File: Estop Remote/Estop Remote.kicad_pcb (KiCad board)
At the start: 2 copper layers, 64.8 x 26.7 mm, 5 parts, among them J1 Enable Out, J2 Power, U1 AdafruitFeatherM0LoRa

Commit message: Estop Remote First Draft
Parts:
- removed the G*** at (144.8, 82.5)
- removed the G*** at (170.2, 82.5)
- added G***: LOGO, SCR_KiCAD_Lib:crab-image, F.Cu at (172.1, 47.6)
- added G***: LOGO, SCR_KiCAD_Lib:scr-logo, B.Cu at (171.4, 115.6)
- added G***: LOGO, SCR_KiCAD_Lib:scr-logo, F.Cu at (171.4, 115.6)
- added SW1: Stop Button, Button_Switch_THT:SW_PUSH_6mm_H5mm, B.Cu at (153.0, 112.4)
- added U2: Nokia5110LED, SCR_KiCAD_Lib:AdafruitNokia5110, B.Cu at (149.9, 63.5)
- J1: value Enable Out -> Power
- J2: value Power -> Kill Signal
- moved J1 40.6 mm to (139.1, 114.9), turned to 180 degrees
- moved J2 28.6 mm to (128.9, 114.9), turned to 180 degrees
- moved U1 15.4 mm to (124.5, 107.3)
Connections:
- J1 pad 2: Net-(J1-Pad2) -> +5V
- J2 pad 2: VCC -> SIG_KILL
- U1 pad 10: Net-(U1-Pad10) -> DSPL_DC
- U1 pad 12: Net-(J1-Pad2) -> DSPL_RST
- U1 pad 13: Net-(U1-Pad13) -> SIG_KILL
- U1 pad 16: VCC -> +5V
- U1 pad 7: Net-(U1-Pad7) -> DSPL_SCLK
- U1 pad 8: Net-(U1-Pad8) -> DSPL_DIN
- U1 pad 9: Net-(U1-Pad9) -> SIG_STOP
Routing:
- net GND: track 0.00 -> 183.6 mm
- net +5V: track 0.00 -> 94.2 mm
- net DSPL_SCLK: track 0.00 -> 51.4 mm
- net DSPL_DIN: track 0.00 -> 51.4 mm
- net DSPL_DC: track 0.00 -> 48.8 mm
- net DSPL_RST: track 0.00 -> 48.8 mm
- net Net-(U2-Pad8): track 0.00 -> 39.4 mm
- net SIG_KILL: track 0.00 -> 38.4 mm
- net Net-(J1-Pad2): track 36.5 -> 0.00 mm
- net SIG_STOP: track 0.00 -> 36.0 mm
- net VCC: track 28.4 -> 0.00 mm
- removed copper zone on B.Cu, net GND
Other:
- board size 64.8 x 26.7 mm -> 55.9 x 82.6 mm
- net class Default: clearance 0.2 -> 0.3
- net class POWER added: clearance 0.4, trace_width 0.5, via_dia 0.8, via_drill 0.4
- rule pad_to_mask_clearance: 0.051 -> 0
- rule trace_clearance: 0.2 -> 0.3
- board text added: "+5V"
- board text added: "Designed by Noah Zemlin Sooner Competitive Robotics"
- board text added: "GND"
- board text added: "KILL"

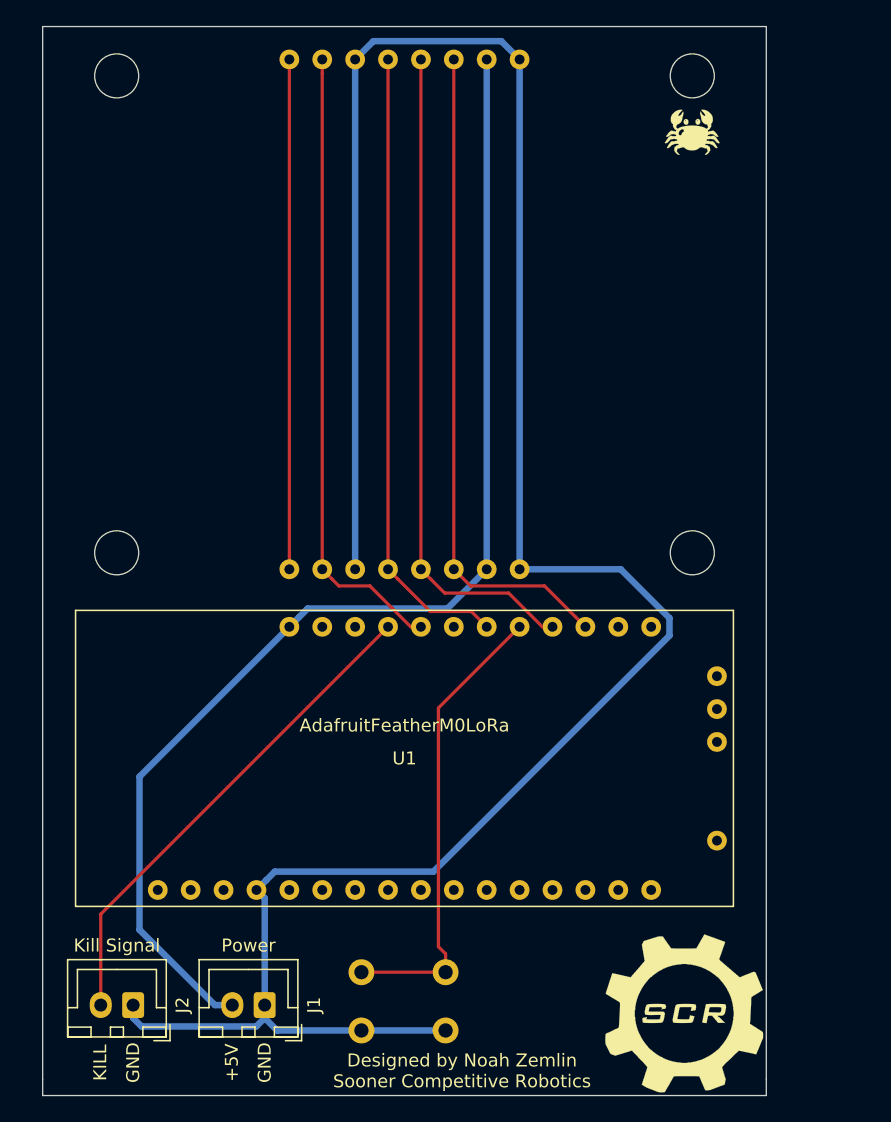
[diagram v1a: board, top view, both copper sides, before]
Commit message: Attached LED pin and fix power delivery
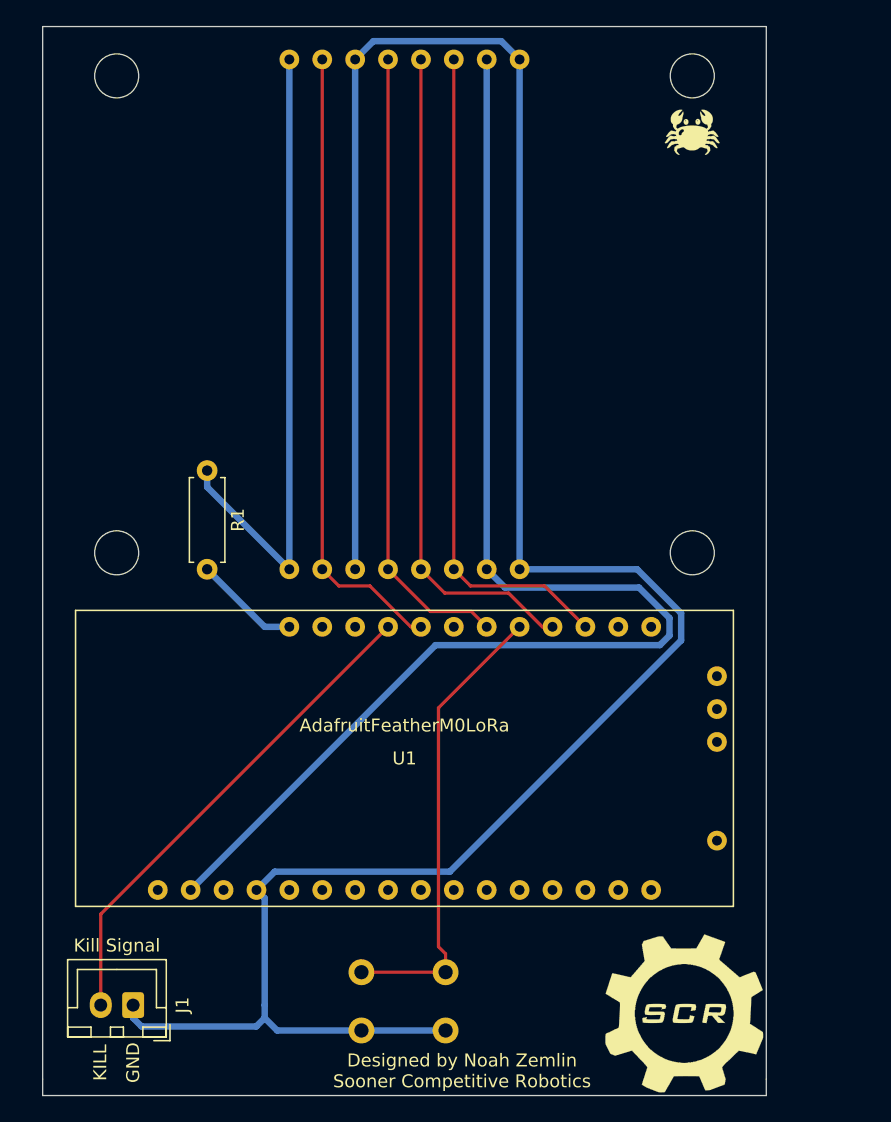
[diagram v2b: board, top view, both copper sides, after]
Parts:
- removed the J1 at (139.1, 114.9)
- added R1: 560, Resistor_THT:R_Axial_DIN0207_L6.3mm_D2.5mm_P7.62mm_Horizontal, F.Cu at (134.6, 73.7)
- renumbered J2 to J1
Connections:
- U1 pad 31: Net-(U1-Pad31) -> +3V3
- U2 pad 2: +5V -> +3V3
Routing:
- net +3V3: track 0.00 -> 101.5 mm
- net +5V: track 94.2 -> 8.19 mm
- net Net-(R1-Pad1): track 39.4 -> 49.6 mm
- net GND: track 183.6 -> 185.6 mm
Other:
- board text removed: "+5V"

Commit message: Added ground plane and Antenna net name
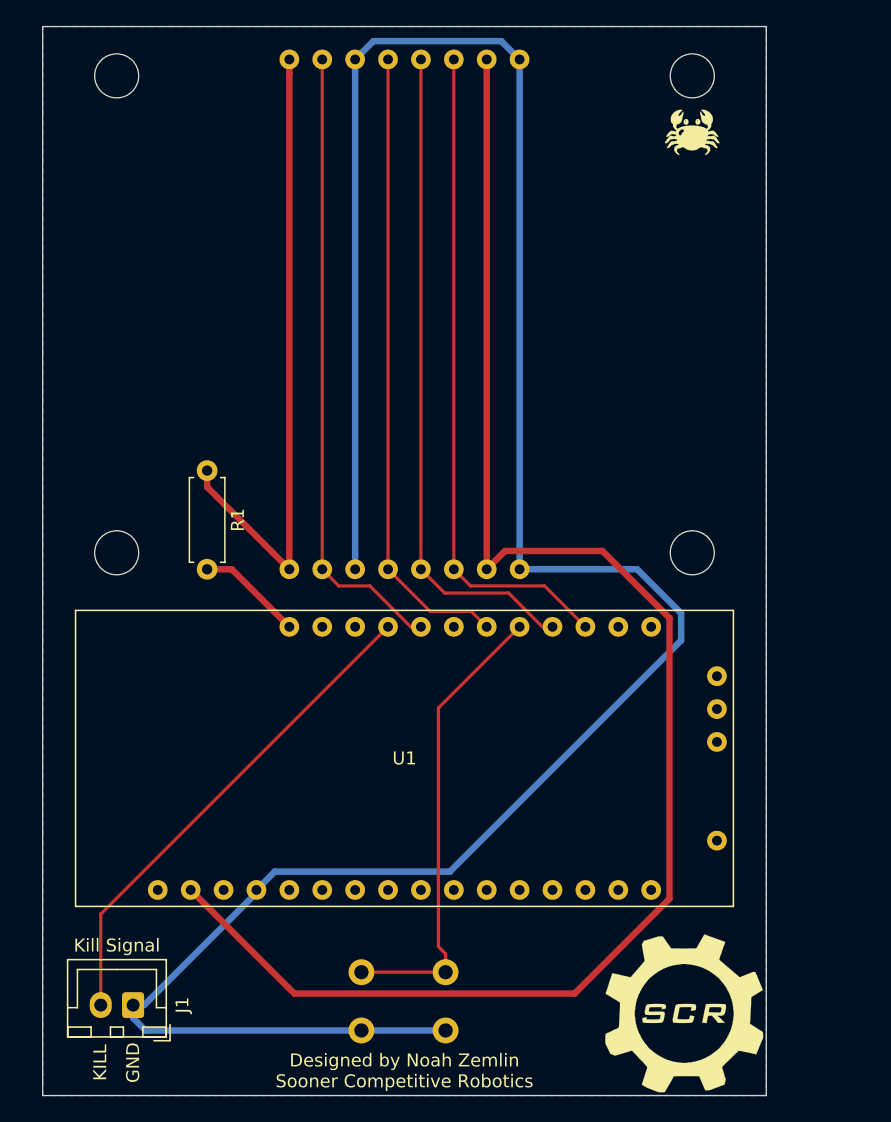
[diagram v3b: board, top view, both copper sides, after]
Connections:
- net Net-(U1-Pad1) renamed ANTENNA
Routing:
- net +3V3: track 101.5 -> 121.2 mm
- net GND: track 185.6 -> 188.2 mm
- added copper zone on B.Cu, net GND
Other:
- net class Atenna added: clearance 0.4, trace_width 1, via_dia 0.8, via_drill 0.4
- net class POWER removed
- net class Power added: clearance 0.4, trace_width 0.5, via_dia 0.8, via_drill 0.4

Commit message: Fixed mounting holes and resistor position
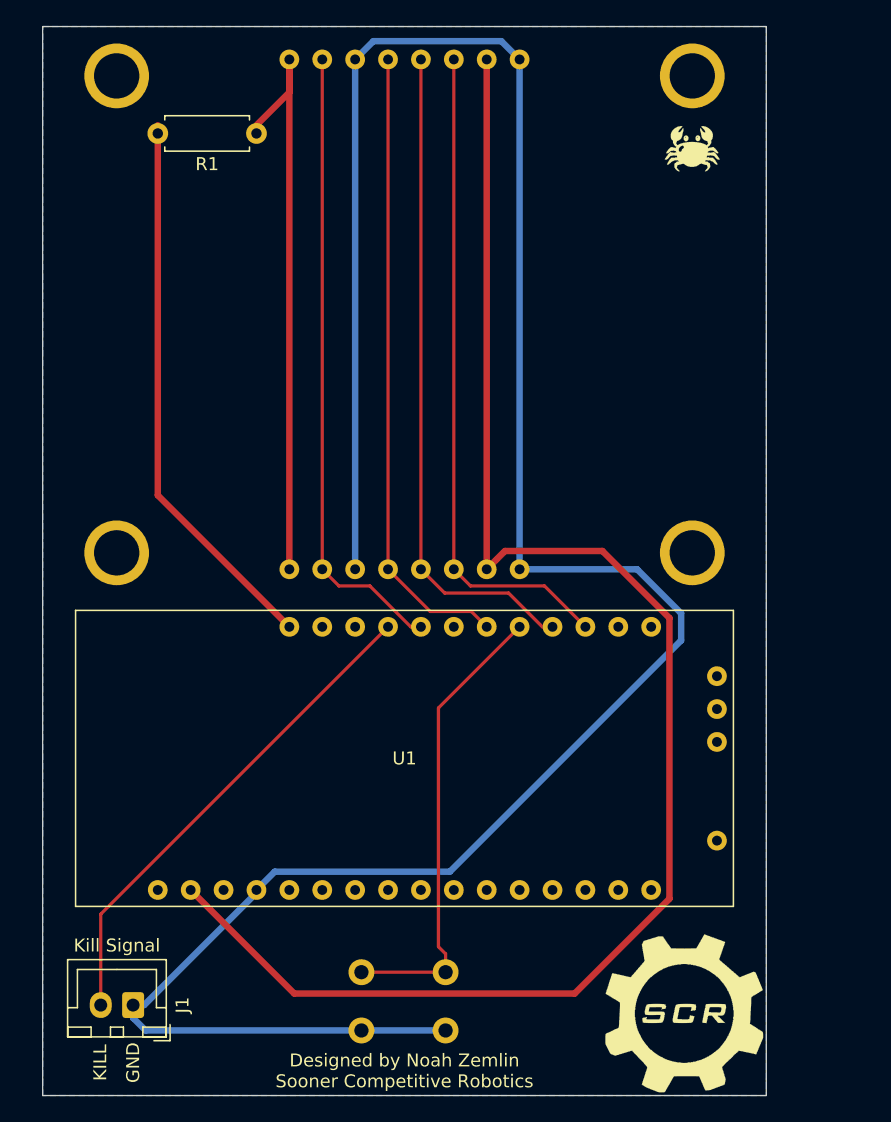
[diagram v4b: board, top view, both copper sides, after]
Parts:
- moved R1 26.3 mm to (138.4, 47.6), turned to 180 degrees
- moved G*** 1.27 mm to (172.1, 48.9)
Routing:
- net +5V: track 8.19 -> 42.9 mm
- net Net-(R1-Pad1): track 49.6 -> 45.5 mm
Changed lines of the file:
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@@
   (layers
     (0 F.Cu signal)
-    (31 B.Cu signal)
+    (31 B.Cu signal hide)
     (32 B.Adhes user)
     (33 F.Adhes user)
@@
     (add_net "Net-(R1-Pad1)")
   )
+  (module SCR_KiCAD_Lib:AdafruitNokia5110 (layer B.Cu)
+    (at 149.86 63.5 180)
+    (fp_text reference U2 (at 0 -2.54) (layer B.SilkS)
+      (effects (font (size 1 1) (thickness 0.15)) (justify mirror))
+    )
+    (fp_text value Nokia5110LED (at 0 0) (layer B.SilkS)
+      (effects (font (size 1 1) (thickness 0.15)) (justify mirror))
+    )
+    (fp_line (start -24.765 22.86) (end -24.765 -19.05) (layer B.SilkS) (width 0.12))
+    (fp_line (start 24.765 22.86) (end -24.765 22.86) (layer B.SilkS) (width 0.12))
+    (fp_line (start 24.765 -19.05) (end 24.765 22.86) (layer B.SilkS) (width 0.12))
+    (fp_line (start -24.765 -19.05) (end 24.765 -19.05) (layer B.SilkS) (width 0.12))
+    (pad "" thru_hole circle (at -22.225 -16.51 180) (size 5 5) (drill 3.5) (layers *.Cu *.Mask))
+    (pad "" thru_hole circle (at 22.225 -16.51 180) (size 5 5) (drill 3.5) (layers *.Cu *.Mask))
+    (pad "" thru_hole circle (at 22.225 20.32 180) (size 5 5) (drill 3.5) (layers *.Cu *.Mask))
+    (pad "" thru_hole circle (at -22.225 20.32 180) (size 5 5) (drill 3.5) (layers *.Cu *.Mask))
+    (pad 5 thru_hole circle (at 1.27 -17.78 180) (size 1.524 1.524) (drill 0.762) (layers *.Cu *.Mask)
+      (net 4 DSPL_DC))
+    (pad 2 thru_hole circle (at -6.35 -17.78 180) (size 1.524 1.524) (drill 0.762) (layers *.Cu *.Mask)
+      (net 31 +3V3))
+    (pad 4 thru_hole circle (at -1.27 -17.78 180) (size 1.524 1.524) (drill 0.762) (layers *.Cu *.Mask)
+      (net 5 DSPL_DIN))
+    (pad 3 thru_hole circle (at -3.81 -17.78 180) (size 1.524 1.524) (drill 0.762) (layers *.Cu *.Mask)
+      (net 6 DSPL_SCLK))
+    (pad 1 thru_hole circle (at -8.89 -17.78 180) (size 1.524 1.524) (drill 0.762) (layers *.Cu *.Mask)
+      (net 1 GND))
+    (pad 6 thru_hole circle (at 3.81 -17.78 180) (size 1.524 1.524) (drill 0.762) (layers *.Cu *.Mask)
+      (net 1 GND))
+    (pad 8 thru_hole circle (at 8.89 -17.78 180) (size 1.524 1.524) (drill 0.762) (layers *.Cu *.Mask)
+      (net 30 "Net-(R1-Pad1)"))
+    (pad 7 thru_hole circle (at 6.35 -17.78 180) (size 1.524 1.524) (drill 0.762) (layers *.Cu *.Mask)
+      (net 3 DSPL_RST))
+    (pad 2 thru_hole circle (at -6.35 21.59 180) (size 1.524 1.524) (drill 0.762) (layers *.Cu *.Mask)
+      (net 31 +3V3))
+    (pad 4 thru_hole circle (at -1.27 21.59 180) (size 1.524 1.524) (drill 0.762) (layers *.Cu *.Mask)
+      (net 5 DSPL_DIN))
+    (pad 1 thru_hole circle (at -8.89 21.59 180) (size 1.524 1.524) (drill 0.762) (layers *.Cu *.Mask)
+      (net 1 GND))
+    (pad 6 thru_hole circle (at 3.81 21.59 180) (size 1.524 1.524) (drill 0.762) (layers *.Cu *.Mask)
+      (net 1 GND))
+    (pad 8 thru_hole circle (at 8.89 21.59 180) (size 1.524 1.524) (drill 0.762) (layers *.Cu *.Mask)
+      (net 30 "Net-(R1-Pad1)"))
+    (pad 7 thru_hole circle (at 6.35 21.59 180) (size 1.524 1.524) (drill 0.762) (layers *.Cu *.Mask)
+      (net 3 DSPL_RST))
+    (pad 5 thru_hole circle (at 1.27 21.59 180) (size 1.524 1.524) (drill 0.762) (layers *.Cu *.Mask)
+      (net 4 DSPL_DC))
+    (pad 3 thru_hole circle (at -3.81 21.59 180) (size 1.524 1.524) (drill 0.762) (layers *.Cu *.Mask)
+      (net 6 DSPL_SCLK))
+  )
   (module SCR_KiCAD_Lib:AdafruitFeatherM0LoRa (layer F.Cu)
     (at 124.46 107.315)
@@
       (net 7 "Net-(U1-Pad32)"))
   )
-  (module SCR_KiCAD_Lib:AdafruitNokia5110 (layer B.Cu)
-    (at 149.86 63.5 180)
-    (fp_text reference U2 (at 0 -2.54) (layer B.SilkS)
-      (effects (font (size 1 1) (thickness 0.15)) (justify mirror))
-    )
-    (fp_text value Nokia5110LED (at 0 0) (layer B.SilkS)
-      (effects (font (size 1 1) (thickness 0.15)) (justify mirror))
-    )
-    (fp_line (start -24.765 22.86) (end -24.765 -19.05) (layer B.SilkS) (width 0.12))
-    (fp_line (start 24.765 22.86) (end -24.765 22.86) (layer B.SilkS) (width 0.12))
-    (fp_line (start 24.765 -19.05) (end 24.765 22.86) (layer B.SilkS) (width 0.12))
-    (fp_line (start -24.765 -19.05) (end 24.765 -19.05) (layer B.SilkS) (width 0.12))
-    (pad "" np_thru_hole circle (at -22.225 -16.51 180) (size 3.4 3.4) (drill 3.4) (layers *.Cu *.Mask))
-    (pad "" np_thru_hole circle (at 22.225 -16.51 180) (size 3.4 3.4) (drill 3.4) (layers *.Cu *.Mask))
-    (pad "" np_thru_hole circle (at 22.225 20.32 180) (size 3.4 3.4) (drill 3.4) (layers *.Cu *.Mask))
-    (pad "" np_thru_hole circle (at -22.225 20.32 180) (size 3.4 3.4) (drill 3.4) (layers *.Cu *.Mask))
-    (pad 5 thru_hole circle (at 1.27 -17.78 180) (size 1.524 1.524) (drill 0.762) (layers *.Cu *.Mask)
-      (net 4 DSPL_DC))
-    (pad 2 thru_hole circle (at -6.35 -17.78 180) (size 1.524 1.524) (drill 0.762) (layers *.Cu *.Mask)
-      (net 31 +3V3))
-    (pad 4 thru_hole circle (at -1.27 -17.78 180) (size 1.524 1.524) (drill 0.762) (layers *.Cu *.Mask)
-      (net 5 DSPL_DIN))
-    (pad 3 thru_hole circle (at -3.81 -17.78 180) (size 1.524 1.524) (drill 0.762) (layers *.Cu *.Mask)
-      (net 6 DSPL_SCLK))
-    (pad 1 thru_hole circle (at -8.89 -17.78 180) (size 1.524 1.524) (drill 0.762) (layers *.Cu *.Mask)
-      (net 1 GND))
-    (pad 6 thru_hole circle (at 3.81 -17.78 180) (size 1.524 1.524) (drill 0.762) (layers *.Cu *.Mask)
-      (net 1 GND))
-    (pad 8 thru_hole circle (at 8.89 -17.78 180) (size 1.524 1.524) (drill 0.762) (layers *.Cu *.Mask)
-      (net 30 "Net-(R1-Pad1)"))
-    (pad 7 thru_hole circle (at 6.35 -17.78 180) (size 1.524 1.524) (drill 0.762) (layers *.Cu *.Mask)
-      (net 3 DSPL_RST))
-    (pad 2 thru_hole circle (at -6.35 21.59 180) (size 1.524 1.524) (drill 0.762) (layers *.Cu *.Mask)
-      (net 31 +3V3))
-    (pad 4 thru_hole circle (at -1.27 21.59 180) (size 1.524 1.524) (drill 0.762) (layers *.Cu *.Mask)
-      (net 5 DSPL_DIN))
-    (pad 1 thru_hole circle (at -8.89 21.59 180) (size 1.524 1.524) (drill 0.762) (layers *.Cu *.Mask)
-      (net 1 GND))
-    (pad 6 thru_hole circle (at 3.81 21.59 180) (size 1.524 1.524) (drill 0.762) (layers *.Cu *.Mask)
-      (net 1 GND))
-    (pad 8 thru_hole circle (at 8.89 21.59 180) (size 1.524 1.524) (drill 0.762) (layers *.Cu *.Mask)
-      (net 30 "Net-(R1-Pad1)"))
-    (pad 7 thru_hole circle (at 6.35 21.59 180) (size 1.524 1.524) (drill 0.762) (layers *.Cu *.Mask)
-      (net 3 DSPL_RST))
-    (pad 5 thru_hole circle (at 1.27 21.59 180) (size 1.524 1.524) (drill 0.762) (layers *.Cu *.Mask)
-      (net 4 DSPL_DC))
-    (pad 3 thru_hole circle (at -3.81 21.59 180) (size 1.524 1.524) (drill 0.762) (layers *.Cu *.Mask)
-      (net 6 DSPL_SCLK))
-  )
   (module Resistor_THT:R_Axial_DIN0207_L6.3mm_D2.5mm_P7.62mm_Horizontal (layer F.Cu)
-    (at 134.62 73.66 270)
+    (at 138.43 47.625 180)
     (descr "Resistor, Axial_DIN0207 series, Axial, Horizontal, pin pitch=7.62mm, 0.25W = 1/4W, length*diameter=6.3*2.5mm^2, http://cdn-reichelt.de/documents/datenblatt/B400/1_4W%23YAG.pdf")
     (tags "Resistor Axial_DIN0207 series Axial Horizontal pin pitch 7.62mm 0.25W = 1/4W length 6.3mm diameter 2.5mm")
-    (fp_text reference R1 (at 3.81 -2.37 90) (layer F.SilkS)
+    (fp_text reference R1 (at 3.81 -2.37) (layer F.SilkS)
       (effects (font (size 1 1) (thickness 0.15)))
     )
-    (fp_text value 560 (at 3.81 2.37 90) (layer F.Fab)
+    (fp_text value 560 (at 3.81 2.37) (layer F.Fab)
       (effects (font (size 1 1) (thickness 0.15)))
     )
-    (fp_text user %R (at 3.81 0 90) (layer F.Fab)
+    (fp_text user %R (at 3.81 0) (layer F.Fab)
       (effects (font (size 1 1) (thickness 0.15)))
     )
@@
     (fp_line (start 0.66 1.25) (end 6.96 1.25) (layer F.Fab) (width 0.1))
     (fp_line (start 0.66 -1.25) (end 0.66 1.25) (layer F.Fab) (width 0.1))
-    (pad 2 thru_hole oval (at 7.62 0 270) (size 1.6 1.6) (drill 0.8) (layers *.Cu *.Mask)
+    (pad 2 thru_hole oval (at 7.62 0 180) (size 1.6 1.6) (drill 0.8) (layers *.Cu *.Mask)
       (net 28 +5V))
-    (pad 1 thru_hole circle (at 0 0 270) (size 1.6 1.6) (drill 0.8) (layers *.Cu *.Mask)
+    (pad 1 thru_hole circle (at 0 0 180) (size 1.6 1.6) (drill 0.8) (layers *.Cu *.Mask)
       (net 30 "Net-(R1-Pad1)"))
     (model ${KISYS3DMOD}/Resistor_THT.3dshapes/R_Axial_DIN0207_L6.3mm_D2.5mm_P7.62mm_Horizontal.wrl
@@
   )
   (module SCR_KiCAD_Lib:crab-image (layer F.Cu)
-    (at 172.085 47.625)
+    (at 172.085 48.895)
     (fp_text reference G*** (at 0 0) (layer F.SilkS) hide
       (effects (font (size 1.524 1.524) (thickness 0.3)))
@@
   (segment (start 154.957001 82.567001) (end 160.672001 82.567001) (width 0.25) (layer F.Cu) (net 6))
   (segment (start 153.67 81.28) (end 154.957001 82.567001) (width 0.25) (layer F.Cu) (net 6) (status 10))
-  (segment (start 136.525 81.28) (end 140.97 85.725) (width 0.5) (layer F.Cu) (net 28))
-  (segment (start 134.62 81.28) (end 136.525 81.28) (width 0.5) (layer F.Cu) (net 28))
+  (segment (start 130.81 75.565) (end 140.97 85.725) (width 0.5) (layer F.Cu) (net 28))
+  (segment (start 130.81 46.99) (end 130.81 75.565) (width 0.5) (layer F.Cu) (net 28))
   (segment (start 153.035 112.395) (end 146.535 112.395) (width 0.25) (layer F.Cu) (net 29) (status 30))
   (segment (start 153.035 110.980787) (end 153.035 112.395) (width 0.25) (layer F.Cu) (net 29) (status 20))
@@
   (segment (start 140.97 42.98763) (end 140.97 81.28) (width 0.5) (layer F.Cu) (net 30))
   (segment (start 140.97 41.91) (end 140.97 42.98763) (width 0.5) (layer F.Cu) (net 30))
-  (segment (start 134.62 74.93) (end 140.97 81.28) (width 0.5) (layer F.Cu) (net 30))
-  (segment (start 134.62 73.66) (end 134.62 74.93) (width 0.5) (layer F.Cu) (net 30))
+  (segment (start 140.97 44.45) (end 138.43 46.99) (width 0.5) (layer F.Cu) (net 30))
+  (segment (start 140.97 41.91) (end 140.97 44.45) (width 0.5) (layer F.Cu) (net 30))
   (segment (start 156.21 41.91) (end 156.21 81.28) (width 0.5) (layer F.Cu) (net 31))
   (segment (start 156.971999 80.518001) (end 156.21 81.28) (width 0.5) (layer F.Cu) (net 31))
